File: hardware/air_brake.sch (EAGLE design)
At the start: 18 parts

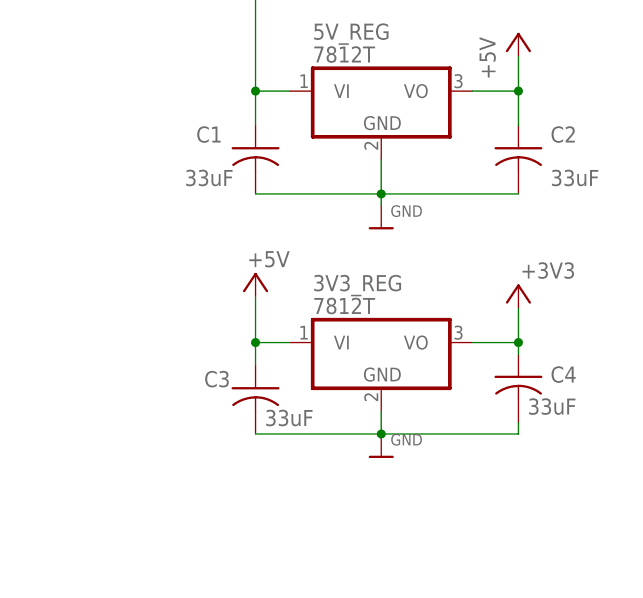
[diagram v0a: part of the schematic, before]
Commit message: updated cap values
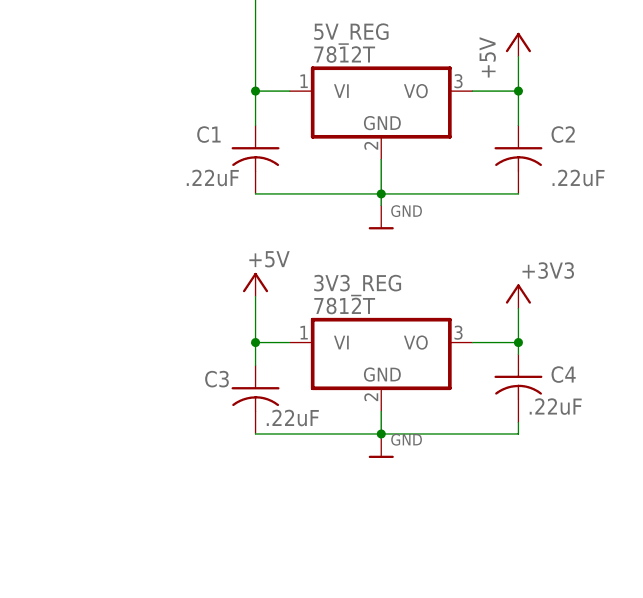
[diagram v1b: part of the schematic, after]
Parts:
- C1, C2, C3, C4: value 33uF -> .22uF
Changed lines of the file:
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@@
 <part name="U$8" library="microbuilder" deviceset="GND" device=""/>
 <part name="U$9" library="microbuilder" deviceset="GND" device=""/>
-<part name="C1" library="adafruit" library_urn="urn:adsk.eagle:library:420" deviceset="C-US" device="025-040X050" package3d_urn="urn:adsk.eagle:package:6240321/1" value="33uF"/>
-<part name="C2" library="adafruit" library_urn="urn:adsk.eagle:library:420" deviceset="C-US" device="025-040X050" package3d_urn="urn:adsk.eagle:package:6240321/1" value="33uF"/>
-<part name="C3" library="adafruit" library_urn="urn:adsk.eagle:library:420" deviceset="C-US" device="025-040X050" package3d_urn="urn:adsk.eagle:package:6240321/1" value="33uF"/>
-<part name="C4" library="adafruit" library_urn="urn:adsk.eagle:library:420" deviceset="C-US" device="025-040X050" package3d_urn="urn:adsk.eagle:package:6240321/1" value="33uF"/>
+<part name="C1" library="adafruit" library_urn="urn:adsk.eagle:library:420" deviceset="C-US" device="025-040X050" package3d_urn="urn:adsk.eagle:package:6240321/1" value=".22uF"/>
+<part name="C2" library="adafruit" library_urn="urn:adsk.eagle:library:420" deviceset="C-US" device="025-040X050" package3d_urn="urn:adsk.eagle:package:6240321/1" value=".22uF"/>
+<part name="C3" library="adafruit" library_urn="urn:adsk.eagle:library:420" deviceset="C-US" device="025-040X050" package3d_urn="urn:adsk.eagle:package:6240321/1" value=".22uF"/>
+<part name="C4" library="adafruit" library_urn="urn:adsk.eagle:library:420" deviceset="C-US" device="025-040X050" package3d_urn="urn:adsk.eagle:package:6240321/1" value=".22uF"/>
 <part name="P+2" library="supply1" deviceset="+5V" device=""/>
 <part name="+3V2" library="supply1" deviceset="+3V3" device=""/>

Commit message: very rough prelim board layout
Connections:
- net N$1: now also TEENSY4.0.11/MOSI; no longer TEENSY4.0.3/PWM
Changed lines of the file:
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@@
 <pinref part="R2" gate="G$1" pin="1"/>
 <pinref part="R1" gate="G$1" pin="1"/>
-<wire x1="43.18" y1="128.27" x2="43.18" y2="130.81" width="0.1524" layer="91" grouprefs="BATTERY_VOLTAGE"/>
-<pinref part="TEENSY4.0" gate="G$1" pin="3/PWM"/>
-<wire x1="111.76" y1="104.14" x2="107.95" y2="104.14" width="0.1524" layer="91"/>
-<wire x1="107.95" y1="104.14" x2="107.95" y2="130.81" width="0.1524" layer="91"/>
-<wire x1="107.95" y1="130.81" x2="43.18" y2="130.81" width="0.1524" layer="91"/>
-<junction x="43.18" y="130.81"/>
+<wire x1="43.18" y1="128.27" x2="43.18" y2="129.54" width="0.1524" layer="91" grouprefs="BATTERY_VOLTAGE"/>
+<pinref part="TEENSY4.0" gate="G$1" pin="11/MOSI"/>
+<wire x1="43.18" y1="129.54" x2="43.18" y2="130.81" width="0.1524" layer="91" grouprefs="BATTERY_VOLTAGE"/>
+<wire x1="111.76" y1="83.82" x2="88.9" y2="83.82" width="0.1524" layer="91"/>
+<wire x1="88.9" y1="83.82" x2="88.9" y2="129.54" width="0.1524" layer="91"/>
+<wire x1="88.9" y1="129.54" x2="43.18" y2="129.54" width="0.1524" layer="91"/>
+<junction x="43.18" y="129.54"/>
 </segment>
 </net>

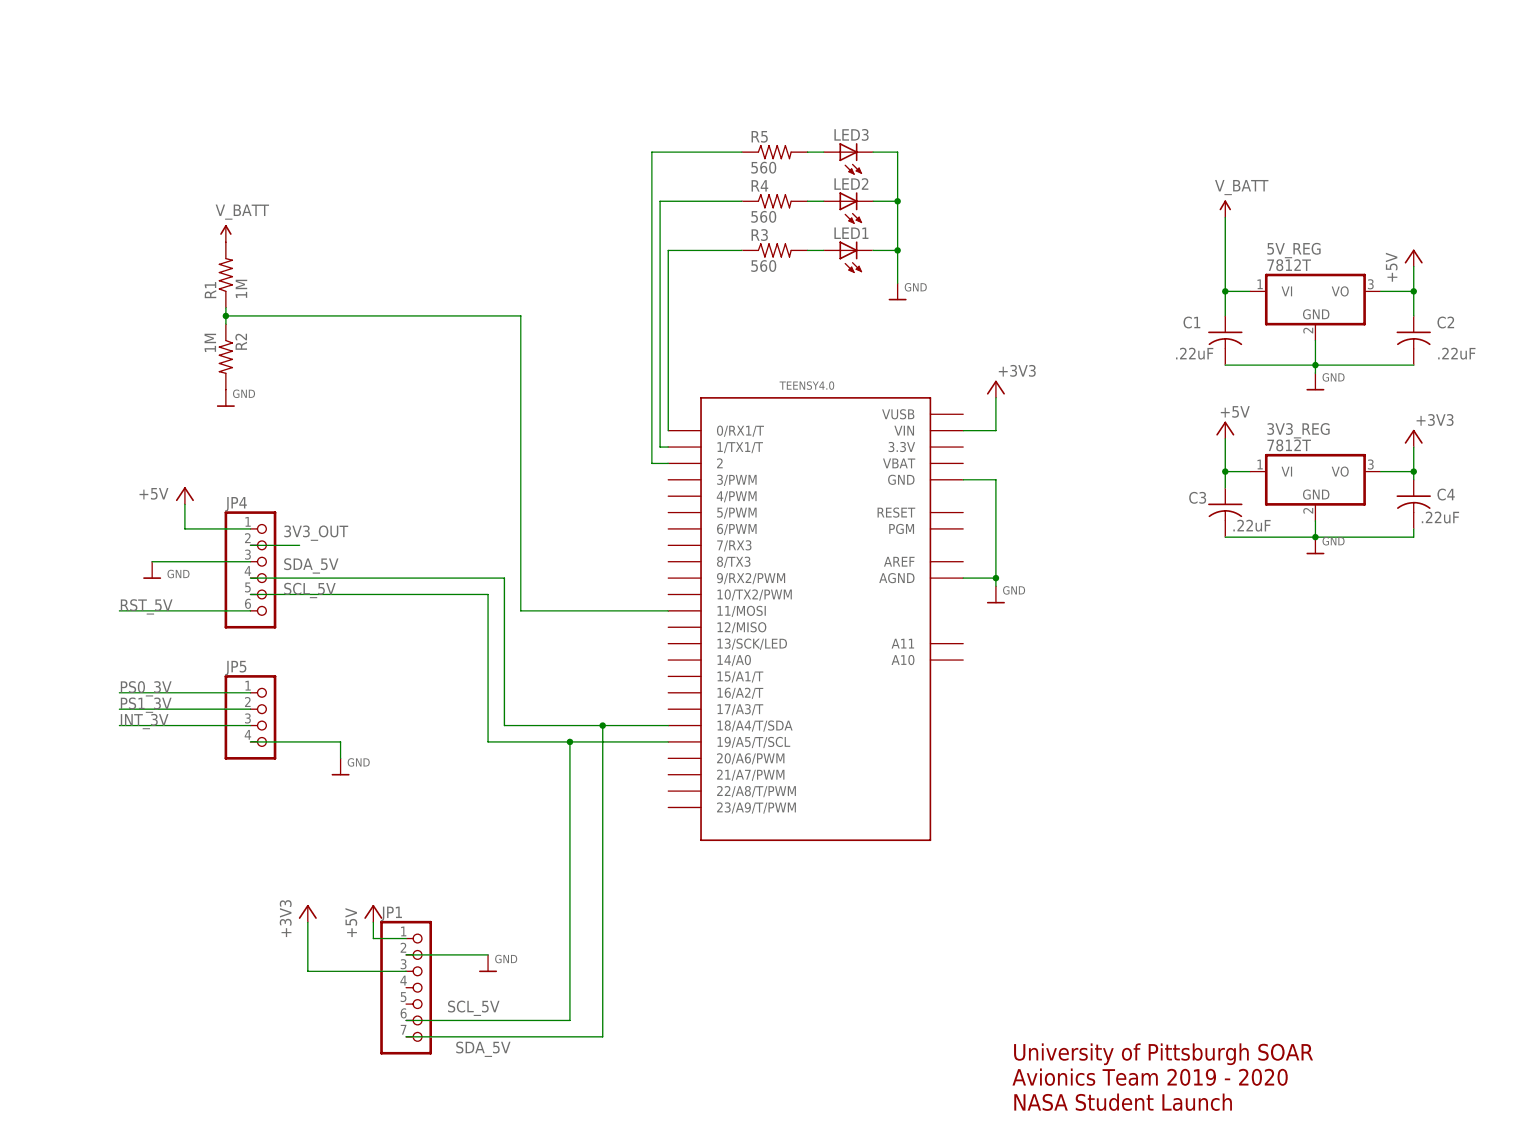
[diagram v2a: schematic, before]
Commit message: updated to reflect no logging
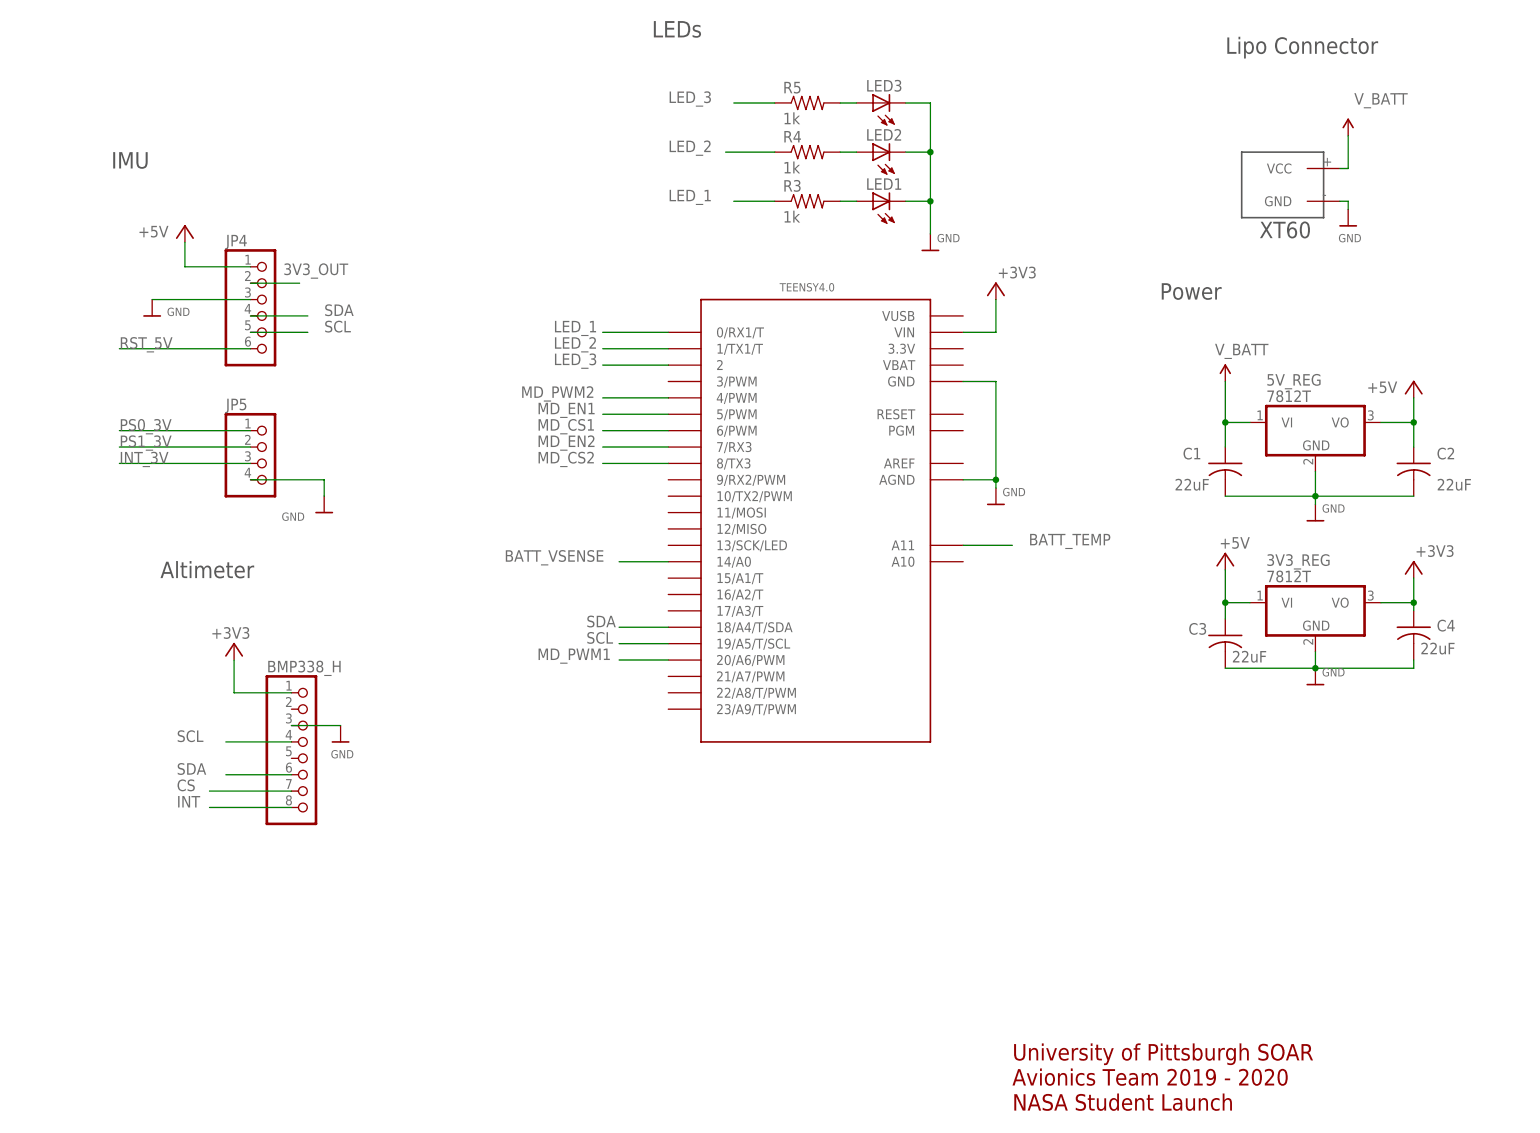
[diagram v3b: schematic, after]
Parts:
- removed JP1: (no value), microbuilder:HEADER-1X770MIL
- removed R1, R2: 1M, resistor:R-US_0309/10
- added BMP338_H: (no value), microbuilder:HEADER-1X870MIL
- added U$1: XT60, XT60:XT60
- C1, C2, C3, C4: value .22uF -> 22uF
- R3, R4, R5: value 560 -> 1k
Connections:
- net N$2 renamed LED_1
- net N$6 renamed LED_2
- net N$7 renamed LED_3
- removed net N$1: R1.1, R2.1, TEENSY4.0.11/MOSI
- removed net SCL_5V: JP1.6, JP4.5, TEENSY4.0.19/A5/T/SCL
- removed net SDA_5V: JP1.7, JP4.4, TEENSY4.0.18/A4/T/SDA
- new net BATT_TEMP: TEENSY4.0.A11
- new net BATT_VSENSE: TEENSY4.0.14/A0
- new net CS: BMP338_H.7
- new net INT: BMP338_H.8
- new net MD_CS1: TEENSY4.0.6/PWM
- new net MD_CS2: TEENSY4.0.8/TX3
- new net MD_EN1: TEENSY4.0.5/PWM
- new net MD_EN2: TEENSY4.0.7/RX3
- new net MD_PWM1: TEENSY4.0.20/A6/PWM
- new net MD_PWM2: TEENSY4.0.4/PWM
- new net SCL: BMP338_H.4, JP4.5, TEENSY4.0.19/A5/T/SCL
- new net SDA: BMP338_H.6, JP4.4, TEENSY4.0.18/A4/T/SDA
- net +3V3: now also BMP338_H.1; no longer JP1.3
- net +5V: no longer JP1.1
- net GND: now also BMP338_H.3, U$1.GND; no longer JP1.2, R2.2
- net V_BATT: now also U$1.VCC; no longer R1.2
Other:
- note added: "Altimeter"
- note added: "IMU"
- note added: "LEDs"
- note added: "Lipo Connector"
- note added: "Power"
- moved on the sheet: 3V3_REG, 5V_REG, C1, C2, C3, C4, JP4, JP5, LED1, LED2, LED3, R3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

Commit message: Changes to Airbrake Sch.
Add 5V and Motor
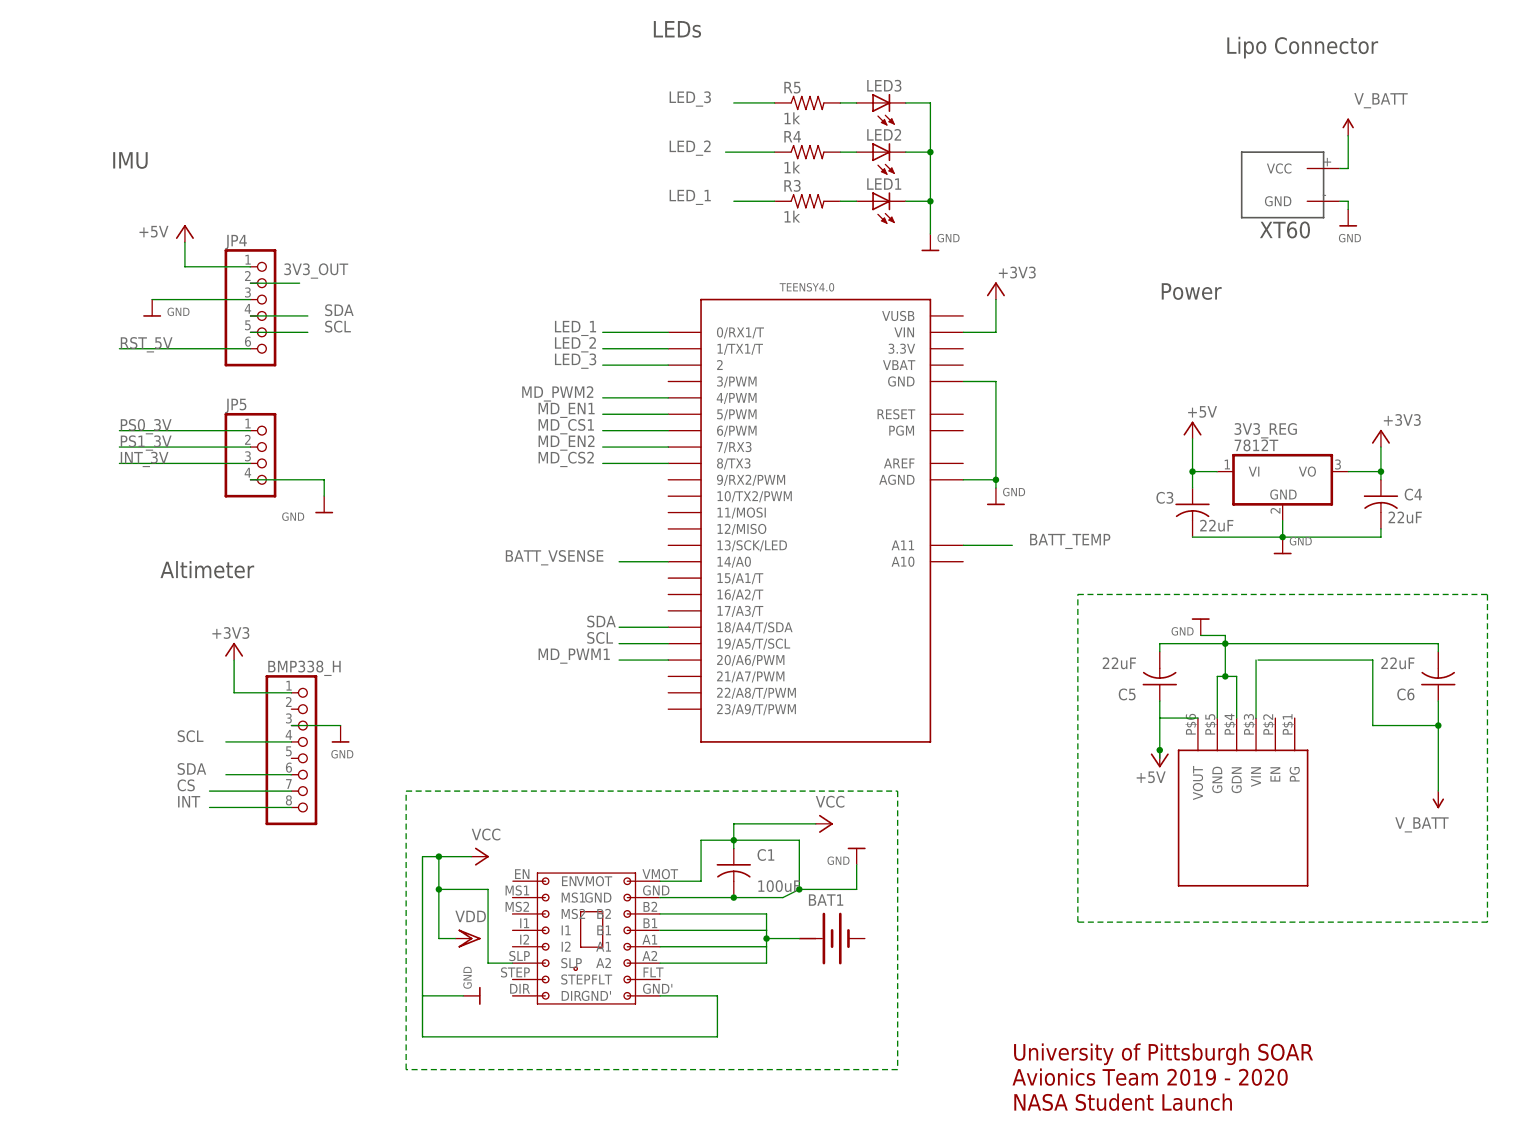
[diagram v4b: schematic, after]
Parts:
- removed 5V_REG: 7812T, adafruit:7812T
- removed C2: 22uF, adafruit:C-US025-040X050
- added BAT1: (no value), special:BATTERY
- added C5, C6: 22uF, adafruit:C-US025-040X050
- added U$4: 5VREGULATOR, Pololu 5V Regulator:5VREGULATOR
- added U$8: MP6500STEPPERMOTORDRIVERCARRIER, MP6500 Stepper Motor Driver Carrier:MP6500STEPPERMOTORDRIVERCARRIER
- C1: value 22uF -> 100uF
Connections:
- new net N$1: BAT1.+, U$8.A1, U$8.A2, U$8.B1, U$8.B2
- new net N$2: U$4.VIN
- new net VCC: C1.1, C1.2, U$8.GND, U$8.GND', U$8.SLP, U$8.VMOT
- net +5V: now also C5.1, U$4.VOUT; no longer 5V_REG.VO, C2.1
- net GND: now also C5.2, C6.2, U$4.GDN, U$4.GND; no longer 5V_REG.GND, C1.2, C2.2
- net V_BATT: now also C6.1; no longer 5V_REG.VI, C1.1
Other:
- moved on the sheet: 3V3_REG, C1, C3, C4

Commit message: Added 5V Reg and stepper motor
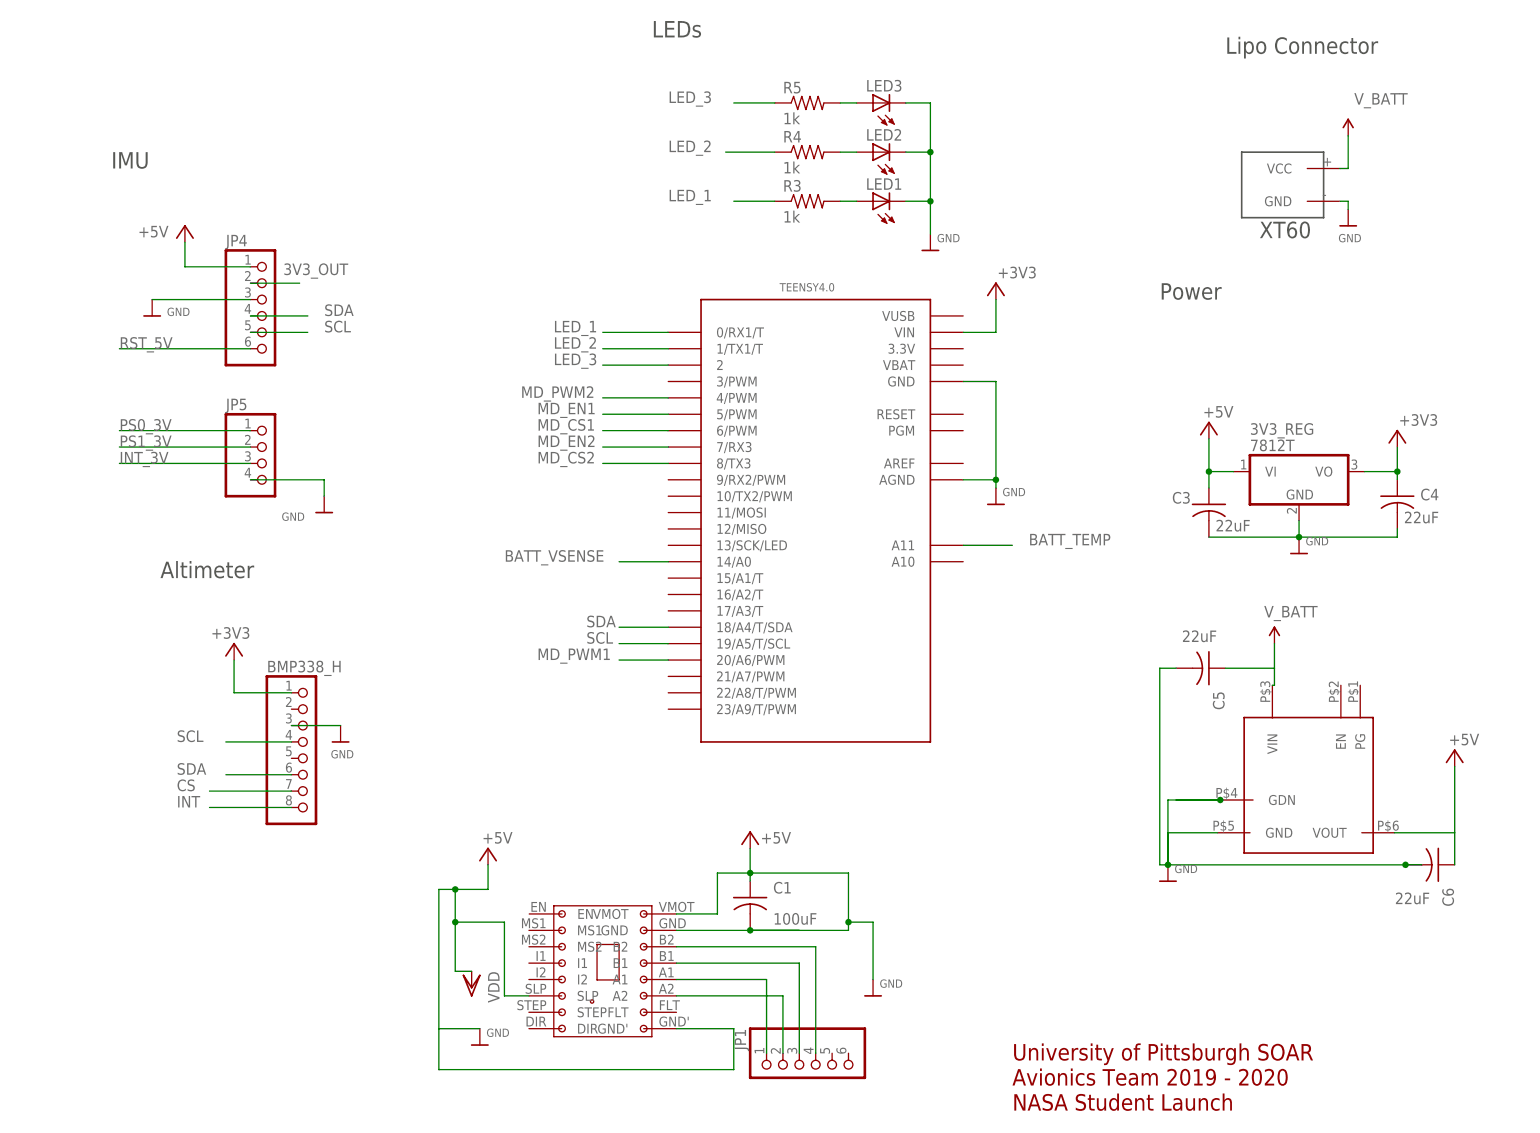
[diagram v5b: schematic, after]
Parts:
- removed BAT1: (no value), special:BATTERY
- added JP1: (no value), pinhead:PINHD-1X6
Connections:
- removed net N$2: U$4.VIN
- removed net VCC: C1.1, C1.2, U$8.GND, U$8.GND', U$8.SLP, U$8.VMOT
- new net N$10: JP1.4, U$8.B2
- new net N$8: JP1.2, U$8.A2
- new net N$9: JP1.3, U$8.B1
- net +5V: now also C1.1, C1.2, C6.1, U$8.GND, U$8.GND', U$8.SLP, U$8.VMOT; no longer C5.1
- net N$1: now also JP1.1; no longer BAT1.+, U$8.A2, U$8.B1, U$8.B2
- net V_BATT: now also C5.1, U$4.VIN; no longer C6.1
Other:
- moved on the sheet: 3V3_REG, C1, C3, C4, C5, C6
